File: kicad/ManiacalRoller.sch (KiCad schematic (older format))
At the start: 1 part

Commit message: Created HDSP-523E Schematic symbol
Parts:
- added SEG?: HDSP-523E, HDSP-523E:HDSP-523E, symbol HDSP-523E
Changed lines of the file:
@@
 LIBS:contrib
 LIBS:valves
+LIBS:HDSP-523E
+LIBS:ManiacalRoller-cache
 EELAYER 25 0
 EELAYER END
@@
 	1    0    0    -1
 $EndComp
+$Comp
+L HDSP-523E SEG?
+U 1 1 589A891F
+P 7000 2500
+F 0 "SEG?" H 7000 3000 50  0000 C CNN
+F 1 "HDSP-523E" H 7000 2050 50  0000 C CNN
+F 2 "HDSP-523E:HDSP-523E" H 7000 1850 50  0000 C CNN
+F 3 "https://docs.broadcom.com/docs/AV02-3586EN" H 7000 1950 50  0000 C CNN
+	1    7000 2500
+	1    0    0    -1
+$EndComp

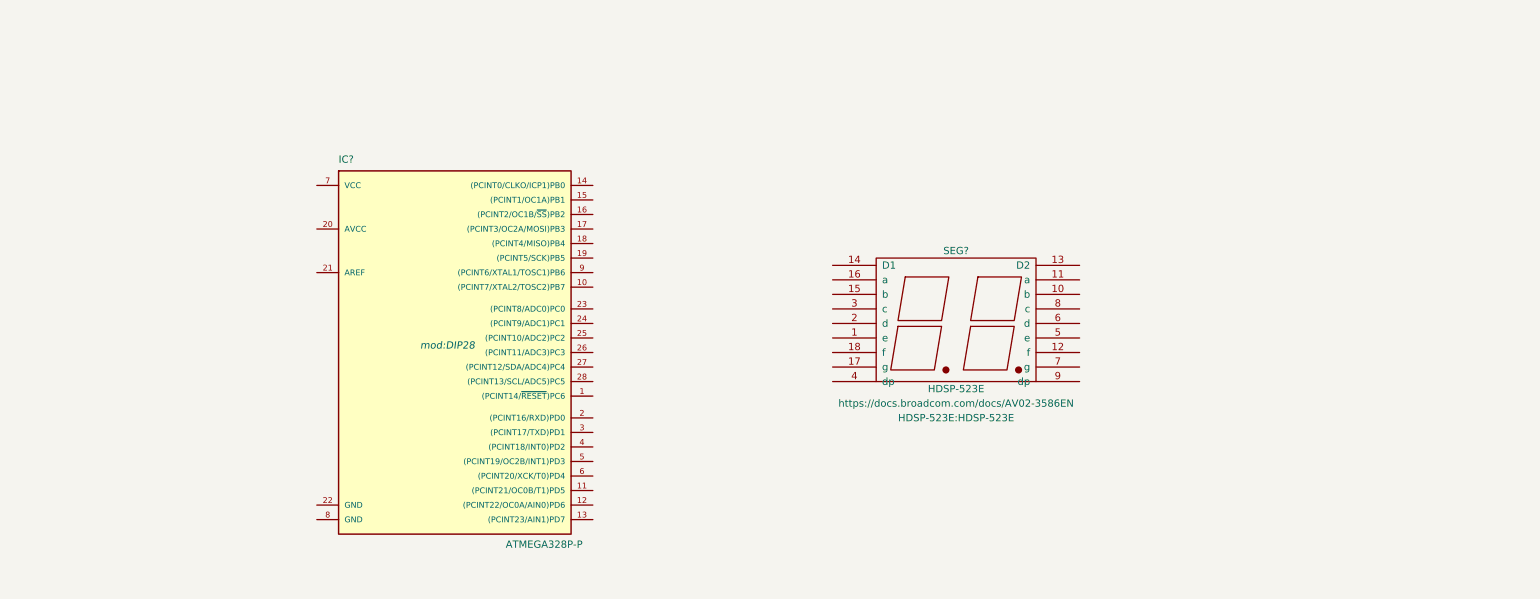
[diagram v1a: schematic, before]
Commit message: Added more components
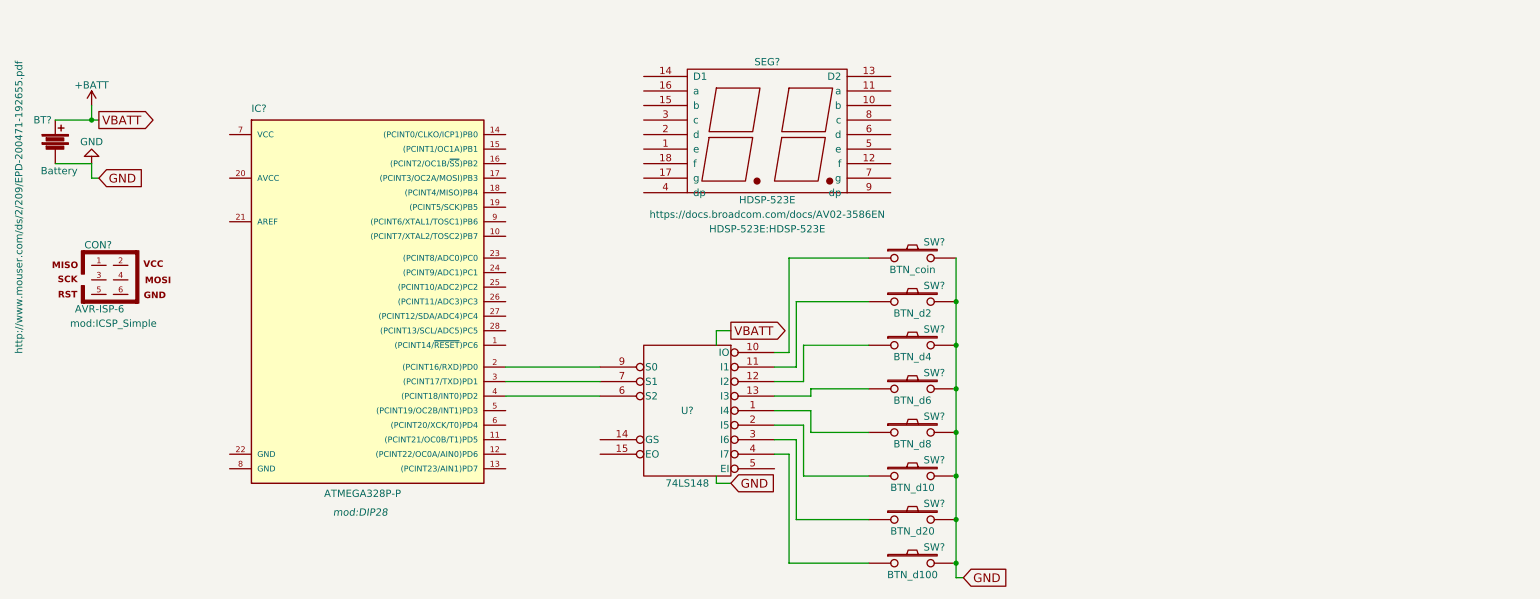
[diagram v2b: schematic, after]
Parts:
- added BT?: Battery, symbol Battery
- added CON?: AVR-ISP-6, mod:ICSP_Simple, symbol AVR-ISP-6
- added SW?: BTN_coin, Buttons_Switches_ThroughHole:SW_PUSH_6mm, symbol SW_PUSH
- added SW?: BTN_d2, Buttons_Switches_ThroughHole:SW_PUSH_6mm, symbol SW_PUSH
- added SW?: BTN_d4, Buttons_Switches_ThroughHole:SW_PUSH_6mm, symbol SW_PUSH
- added SW?: BTN_d6, Buttons_Switches_ThroughHole:SW_PUSH_6mm, symbol SW_PUSH
- added SW?: BTN_d8, Buttons_Switches_ThroughHole:SW_PUSH_6mm, symbol SW_PUSH
- added SW?: BTN_d10, Buttons_Switches_ThroughHole:SW_PUSH_6mm, symbol SW_PUSH
- added SW?: BTN_d20, Buttons_Switches_ThroughHole:SW_PUSH_6mm, symbol SW_PUSH
- added SW?: BTN_d100, Buttons_Switches_ThroughHole:SW_PUSH_6mm, symbol SW_PUSH
- added U?: 74LS148, Housings_DIP:DIP-16_W7.62mm_Socket_LongPads, symbol 74LS148
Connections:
- net at IC?.2 ((PCINT16/RXD)PD0): now also U?.9 (S0)
- net at IC?.3 ((PCINT17/TXD)PD1): now also U?.7 (S1)
- net at IC?.4 ((PCINT18/INT0)PD2): now also U?.6 (S2)
- new net: SW?.1, U?.10 (IO)
- new net: SW?.1, U?.1 (I4)
- new net: SW?.1, U?.11 (I1)
- new net: SW?.1, U?.12 (I2)
- new net: SW?.1, U?.13 (I3)
- new net: SW?.1, U?.2 (I5)
- new net: SW?.1, U?.3 (I6)
- new net: SW?.1, U?.4 (I7)
- new net +BATT: BT?.1, U?.16 (VCC)
- new net GND: BT?.2, SW?.2, SW?.2, SW?.2, SW?.2, SW?.2, SW?.2, SW?.2, SW?.2, U?.8 (GND)
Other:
- moved on the sheet: IC?, SEG?

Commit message: Added to schematic
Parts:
- added C? (x2): 0.1uF, Capacitors_ThroughHole:C_Disc_D3.0mm_W1.6mm_P2.50mm, symbol C
- added Q? (x2): Q_NPN_EBC, TO_SOT_Packages_THT:TO-92_Inline_Narrow_Oval, symbol Q_NPN_EBC
- added R? (x8): 100k, Resistors_ThroughHole:R_Axial_DIN0204_L3.6mm_D1.6mm_P5.08mm_Horizontal, symbol R
- added R? (x2): 1.2k, Resistors_ThroughHole:R_Axial_DIN0204_L3.6mm_D1.6mm_P5.08mm_Horizontal, symbol R
- added R? (x8): 100, Resistors_ThroughHole:R_Axial_DIN0204_L3.6mm_D1.6mm_P5.08mm_Horizontal, symbol R
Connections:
- net +BATT: now also CON?.2, IC?.20 (AVCC), IC?.21 (AREF), IC?.7 (VCC), C?.1, C?.1, R?.2, R?.2, R?.2, R?.2, R?.2, R?.2, R?.2, R?.2
- net GND: now also CON?.6, IC?.22 (GND), IC?.8 (GND), C?.2, C?.2, Q?.1 (E), Q?.1 (E)
- net RST: now reaches IC?.1 ((PCINT14/~RESET~)PC6)
- net RST: now also CON?.5
- net at IC?.10 ((PCINT7/XTAL2/TOSC2)PB7): now also R?.2
- net at IC?.14 ((PCINT0/CLKO/ICP1)PB0): now also R?.2
- net at IC?.15 ((PCINT1/OC1A)PB1): now also R?.2
- net at IC?.16 ((PCINT2/OC1B/~SS~)PB2): now also R?.2
- net MOSI: now reaches IC?.17 ((PCINT3/OC2A/MOSI)PB3)
- net MOSI: now also CON?.4, R?.2
- net MISO: now reaches IC?.18 ((PCINT4/MISO)PB4)
- net MISO: now also CON?.1, R?.2
- net SCK: now reaches IC?.19 ((PCINT5/SCK)PB5)
- net SCK: now also CON?.3, R?.2
- net TENS: now reaches IC?.23 ((PCINT8/ADC0)PC0)
- net TENS: now also R?.2
- net ONES: now reaches IC?.24 ((PCINT9/ADC1)PC1)
- net ONES: now also R?.2
- net at IC?.5 ((PCINT19/OC2B/INT1)PD3): now also U?.15 (EO)
- net at IC?.9 ((PCINT6/XTAL1/TOSC1)PB6): now also R?.2
- net e: now reaches SEG?.1 (e)
- net e: now also SEG?.5 (e), R?.1
- net b: now reaches SEG?.10 (b)
- net b: now also SEG?.15 (b), R?.1
- net a: now reaches SEG?.11 (a)
- net a: now also SEG?.16 (a), R?.1
- net f: now reaches SEG?.12 (f)
- net f: now also SEG?.18 (f), R?.1
- net D2: now reaches SEG?.13 (D2)
- net D2: now also Q?.3 (C)
- net D1: now reaches SEG?.14 (D1)
- net D1: now also Q?.3 (C)
- net g: now reaches SEG?.17 (g)
- net g: now also SEG?.7 (g), R?.1
- net d: now reaches SEG?.2 (d)
- net d: now also SEG?.6 (d), R?.1
- net c: now reaches SEG?.3 (c)
- net c: now also SEG?.8 (c), R?.1
- net dp: now reaches SEG?.4 (dp)
- net dp: now also SEG?.9 (dp), R?.1
- net at SW?.1, U?.10 (IO): now also R?.1
- net at SW?.1, U?.1 (I4): now also R?.1
- net at SW?.1, U?.11 (I1): now also R?.1
- net at SW?.1, U?.12 (I2): now also R?.1
- net at SW?.1, U?.13 (I3): now also R?.1
- net at SW?.1, U?.2 (I5): now also R?.1
- net at SW?.1, U?.3 (I6): now also R?.1
- net at SW?.1, U?.4 (I7): now also R?.1
- new net: Q?.2 (B), R?.1 (x2)
- no-connect marks 0 -> 1
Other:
- moved on the sheet: CON?, SEG?

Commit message: PCB Layout
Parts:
- added R9: 100, Resistors_ThroughHole:R_Axial_DIN0204_L3.6mm_D1.6mm_P5.08mm_Horizontal, symbol R
- BT1: renamed from BT?; footprint (none) -> BattHolder:2xAABatteryHolder_24mm5x53mm
- SW2: renamed from SW?; value BTN_d2 -> BTN_d4
- SW3: renamed from SW?; value BTN_d4 -> BTN_d6
- SW4: renamed from SW?; value BTN_d6 -> BTN_d8
- SW5: renamed from SW?; value BTN_d8 -> BTN_d10
- SW6: renamed from SW?; value BTN_d10 -> BTN_d12
- gave numbers to parts that had none: 29
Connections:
- net GND: now also R9.2
- net at IC1.5 ((PCINT19/OC2B/INT1)PD3), U1.15 (EO): now also R9.1
- no-connect marks 1 -> 10
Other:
- moved on the sheet: Q1, Q2, R18, R19, SEG1

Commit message: Bat Hlder on back
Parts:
- R9: value 100 -> 100K
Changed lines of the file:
@@
 P 4350 3400
 F 0 "R9" V 4300 3250 50  0000 C CNN
-F 1 "100" V 4350 3400 50  0000 C CNN
+F 1 "100K" V 4350 3400 50  0000 C CNN
 F 2 "Resistors_ThroughHole:R_Axial_DIN0204_L3.6mm_D1.6mm_P5.08mm_Horizontal" V 4280 3400 50  0001 C CNN
 F 3 "" H 4350 3400 50  0000 C CNN
